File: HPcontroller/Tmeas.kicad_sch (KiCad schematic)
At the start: 8 parts

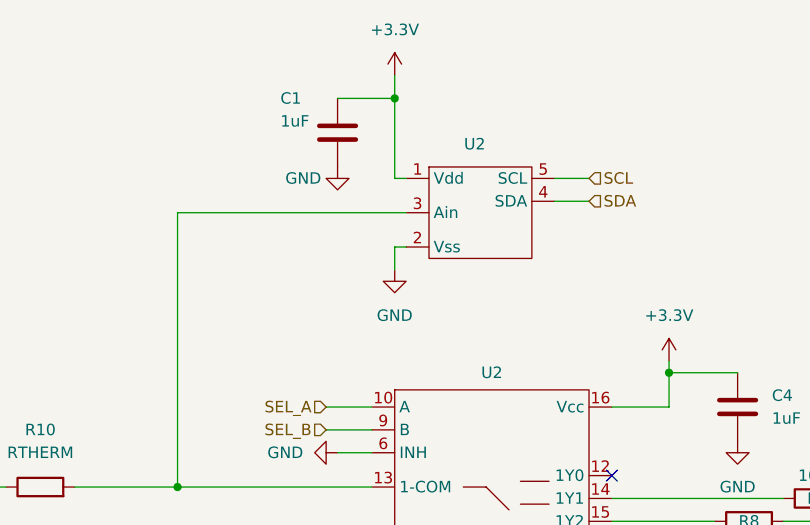
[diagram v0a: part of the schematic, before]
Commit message: started routing, finished footprintns
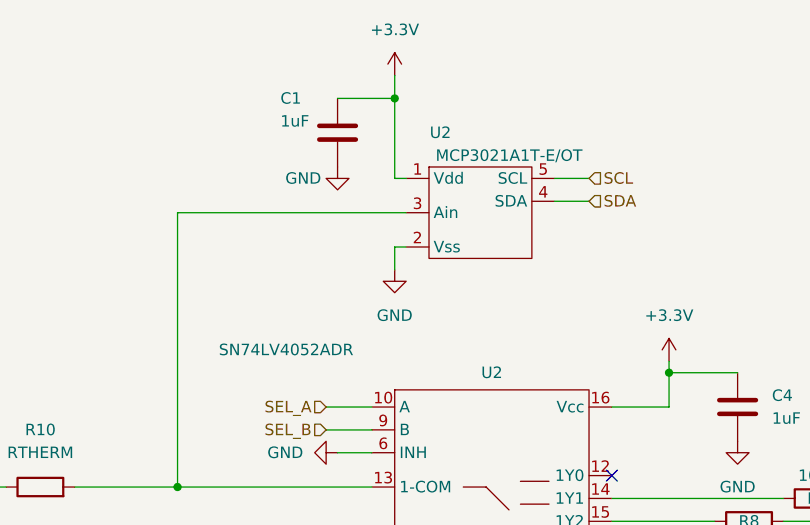
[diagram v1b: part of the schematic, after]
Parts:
- U2: value ~ -> MCP3021A1T-E/OT; footprint (none) -> Package_TO_SOT_SMD:SOT-23-5
- U2: value ~ -> SN74LV4052ADR; footprint (none) -> Package_SO:SOIC-16_3.9x9.9mm_P1.27mm
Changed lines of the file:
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@@
   )
   (symbol (lib_id "HPsym:MCP3021A1T-E/OT") (at 129.54 36.83 0) (unit 1)
-    (in_bom yes) (on_board yes) (dnp no) (fields_autoplaced)
-    (property "Reference" "U2" (at 129.54 34.29 0)
+    (in_bom yes) (on_board yes) (dnp no)
+    (property "Reference" "U2" (at 125.73 33.02 0)
       (effects (font (size 1.27 1.27)))
     )
-    (property "Value" "~" (at 123.825 36.83 0)
+    (property "Value" "MCP3021A1T-E/OT" (at 133.35 35.56 0)
       (effects (font (size 1.27 1.27)))
     )
-    (property "Footprint" "" (at 123.825 36.83 0)
+    (property "Footprint" "Package_TO_SOT_SMD:SOT-23-5" (at 123.825 36.83 0)
       (effects (font (size 1.27 1.27)) hide)
     )
@@
       (effects (font (size 1.27 1.27)))
     )
-    (property "Value" "~" (at 108.585 57.15 0)
+    (property "Value" "SN74LV4052ADR" (at 108.585 57.15 0)
       (effects (font (size 1.27 1.27)))
     )
-    (property "Footprint" "" (at 108.585 57.15 0)
+    (property "Footprint" "Package_SO:SOIC-16_3.9x9.9mm_P1.27mm" (at 108.585 57.15 0)
       (effects (font (size 1.27 1.27)) hide)
     )

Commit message: finished routing, moving on to heater
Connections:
- net +3.3V renamed +3V3
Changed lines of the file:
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@@
-    )
-  )
-  (symbol (lib_id "power:+3.3V") (at 66.04 63.5 0) (unit 1)
-    (in_bom yes) (on_board yes) (dnp no) (fields_autoplaced)
-    (property "Reference" "#PWR038" (at 66.04 67.31 0)
-      (effects (font (size 1.27 1.27)) hide)
-    )
-    (property "Value" "+3.3V" (at 66.04 58.42 0)
-      (effects (font (size 1.27 1.27)))
-    )
-    (property "Footprint" "" (at 66.04 63.5 0)
-      (effects (font (size 1.27 1.27)) hide)
-    )
-    (property "Datasheet" "" (at 66.04 63.5 0)
-      (effects (font (size 1.27 1.27)) hide)
-    )
-    (pin "1")
-    (instances
-      (project "HPcontroller"
-        (path "/e63e39d7-6ac0-4ffd-8aa3-1841a4541b55/1e79cfd4-57e0-46dc-a3a8-eabf19cd908e"
-          (reference "#PWR038") (unit 1)
-        )
-      )
     )
   )
@@
     )
   )
-  (symbol (lib_id "power:+3.3V") (at 151.13 58.42 0) (unit 1)
-    (in_bom yes) (on_board yes) (dnp no) (fields_autoplaced)
-    (property "Reference" "#PWR034" (at 151.13 62.23 0)
-      (effects (font (size 1.27 1.27)) hide)
-    )
-    (property "Value" "+3.3V" (at 151.13 53.34 0)
-      (effects (font (size 1.27 1.27)))
-    )
-    (property "Footprint" "" (at 151.13 58.42 0)
-      (effects (font (size 1.27 1.27)) hide)
-    )
-    (property "Datasheet" "" (at 151.13 58.42 0)
-      (effects (font (size 1.27 1.27)) hide)
-    )
-    (pin "1")
-    (instances
-      (project "HPcontroller"
-        (path "/e63e39d7-6ac0-4ffd-8aa3-1841a4541b55/1e79cfd4-57e0-46dc-a3a8-eabf19cd908e"
-          (reference "#PWR034") (unit 1)
+  (symbol (lib_id "power:+3V3") (at 66.04 63.5 0) (unit 1)
+    (in_bom yes) (on_board yes) (dnp no) (fields_autoplaced)
+    (property "Reference" "#PWR018" (at 66.04 67.31 0)
+      (effects (font (size 1.27 1.27)) hide)
+    )
+    (property "Value" "+3V3" (at 66.04 58.42 0)
+      (effects (font (size 1.27 1.27)))
+    )
+    (property "Footprint" "" (at 66.04 63.5 0)
+      (effects (font (size 1.27 1.27)) hide)
+    )
+    (property "Datasheet" "" (at 66.04 63.5 0)
+      (effects (font (size 1.27 1.27)) hide)
+    )
+    (pin "1")
+    (instances
+      (project "HPcontroller"
+        (path "/e63e39d7-6ac0-4ffd-8aa3-1841a4541b55/1e79cfd4-57e0-46dc-a3a8-eabf19cd908e"
+          (reference "#PWR018") (unit 1)
         )
       )
@@
     )
   )
+  (symbol (lib_id "power:+3V3") (at 151.13 58.42 0) (unit 1)
+    (in_bom yes) (on_board yes) (dnp no) (fields_autoplaced)
+    (property "Reference" "#PWR034" (at 151.13 62.23 0)
+      (effects (font (size 1.27 1.27)) hide)
+    )
+    (property "Value" "+3V3" (at 151.13 53.34 0)
+      (effects (font (size 1.27 1.27)))
+    )
+    (property "Footprint" "" (at 151.13 58.42 0)
+      (effects (font (size 1.27 1.27)) hide)
+    )
+    (property "Datasheet" "" (at 151.13 58.42 0)
+      (effects (font (size 1.27 1.27)) hide)
+    )
+    (pin "1")
+    (instances
+      (project "HPcontroller"
+        (path "/e63e39d7-6ac0-4ffd-8aa3-1841a4541b55/1e79cfd4-57e0-46dc-a3a8-eabf19cd908e"
+          (reference "#PWR034") (unit 1)
+        )
+      )
+    )
+  )
   (symbol (lib_id "power:GND") (at 171.45 82.55 0) (unit 1)
     (in_bom yes) (on_board yes) (dnp no) (fields_autoplaced)
@@
         (path "/e63e39d7-6ac0-4ffd-8aa3-1841a4541b55/1e79cfd4-57e0-46dc-a3a8-eabf19cd908e"
           (reference "#PWR035") (unit 1)
+        )
+      )
+    )
+  )
+  (symbol (lib_id "power:+3V3") (at 120.65 26.67 0) (unit 1)
+    (in_bom yes) (on_board yes) (dnp no) (fields_autoplaced)
+    (property "Reference" "#PWR038" (at 120.65 30.48 0)
+      (effects (font (size 1.27 1.27)) hide)
+    )
+    (property "Value" "+3V3" (at 120.65 21.59 0)
+      (effects (font (size 1.27 1.27)))
+    )
+    (property "Footprint" "" (at 120.65 26.67 0)
+      (effects (font (size 1.27 1.27)) hide)
+    )
+    (property "Datasheet" "" (at 120.65 26.67 0)
+      (effects (font (size 1.27 1.27)) hide)
+    )
+    (pin "1")
+    (instances
+      (project "HPcontroller"
+        (path "/e63e39d7-6ac0-4ffd-8aa3-1841a4541b55/1e79cfd4-57e0-46dc-a3a8-eabf19cd908e"
+          (reference "#PWR038") (unit 1)
         )
       )
@@
         )
       )
-    )
-  )
-  (symbol (lib_id "power:+3.3V") (at 120.65 26.67 0) (unit 1)
-    (in_bom yes) (on_board yes) (dnp no) (fields_autoplaced)
-    (property "Reference" "#PWR039" (at 120.65 30.48 0)
-      (effects (font (size 1.27 1.27)) hide)
-    )
-    (property "Value" "+3.3V" (at 120.65 21.59 0)
-      (effects (font (size 1.27 1.27)))
-    )
-    (property "Footprint" "" (at 120.65 26.67 0)
-      (effects (font (size 1.27 1.27)) hide)
-    )
-    (property "Datasheet" "" (at 120.65 26.67 0)
-      (effects (font (size 1.27 1.27)) hide)
-    )
-    (pin "1")
-    (instances
-      (project "HPcontroller"
-        (path "/e63e39d7-6ac0-4ffd-8aa3-1841a4541b55/1e79cfd4-57e0-46dc-a3a8-eabf19cd908e"
-          (reference "#PWR039") (unit 1)
-        )
-      )

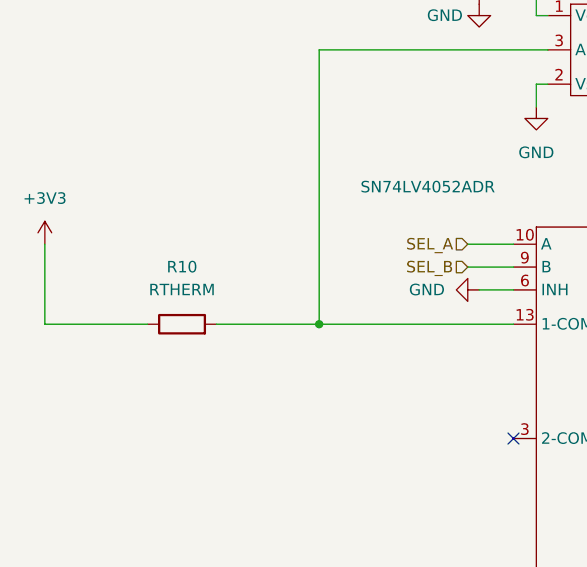
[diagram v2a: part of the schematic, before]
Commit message: worked on bom, orderables from dk are in
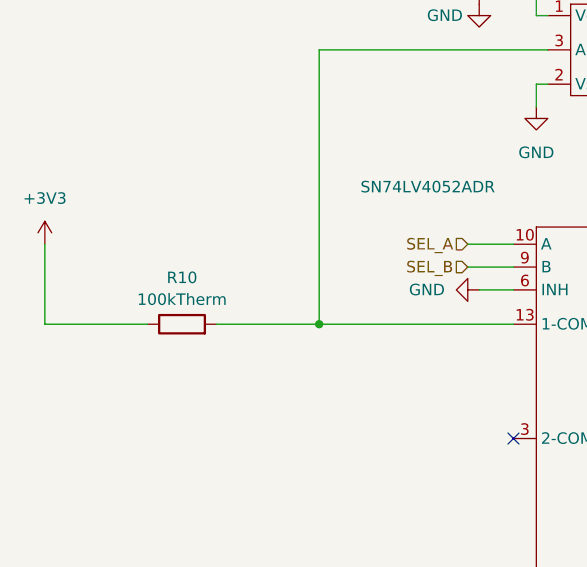
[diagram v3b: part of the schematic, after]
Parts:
- C1, C4: Digikey PN (none) -> 1276-1066-1-ND; MPN (none) -> CL21B105KAFNNNE
- R10: value RTHERM -> 100kTherm; MPN (none) -> 104NT-4-R025H42G
- R7: Digikey PN (none) -> RMCF0805FT100KCT-ND; MPN (none) -> RMCF0805FT100K
- R8: Digikey PN (none) -> RNCP0805FTD10K0CT-ND; MPN (none) -> RNCP0805FTD10K0
- R9: Digikey PN (none) -> RNCP0805FTD1K00CT-ND; MPN (none) -> RNCP0805FTD1K00
- U2: Digikey PN (none) -> MCP3021A1T-E/OTCT-ND; MPN (none) -> MCP3021A1T-E/OT
- U2: Digikey PN (none) -> 296-16707-1-ND; MPN (none) -> SN74LV4052ADR
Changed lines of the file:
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@@
   (symbol (lib_id "Device:R") (at 81.28 72.39 90) (unit 1)
     (in_bom yes) (on_board yes) (dnp no) (fields_autoplaced)
-    (property "Reference" "R10" (at 81.28 66.04 90)
-      (effects (font (size 1.27 1.27)))
-    )
-    (property "Value" "RTHERM" (at 81.28 68.58 90)
+    (property "Reference" "R10" (at 81.28 67.2297 90)
+      (effects (font (size 1.27 1.27)))
+    )
+    (property "Value" "100kTherm" (at 81.28 69.6539 90)
       (effects (font (size 1.27 1.27)))
     )
@@
     )
     (property "Datasheet" "~" (at 81.28 72.39 0)
+      (effects (font (size 1.27 1.27)) hide)
+    )
+    (property "MPN" "104NT-4-R025H42G" (at 81.28 72.39 0)
       (effects (font (size 1.27 1.27)) hide)
     )
@@
       (effects (font (size 1.27 1.27)) hide)
     )
+    (property "Digikey PN" "RNCP0805FTD1K00CT-ND" (at 152.4 78.74 0)
+      (effects (font (size 1.27 1.27)) hide)
+    )
+    (property "MPN" "RNCP0805FTD1K00" (at 152.4 78.74 0)
+      (effects (font (size 1.27 1.27)) hide)
+    )
     (pin "1")
     (pin "2")
@@
       (effects (font (size 1.27 1.27)) hide)
     )
+    (property "Digikey PN" "RNCP0805FTD10K0CT-ND" (at 160.02 76.2 0)
+      (effects (font (size 1.27 1.27)) hide)
+    )
+    (property "MPN" "RNCP0805FTD10K0" (at 160.02 76.2 0)
+      (effects (font (size 1.27 1.27)) hide)
+    )
     (pin "1")
     (pin "2")
@@
     )
     (property "Datasheet" "" (at 123.825 36.83 0)
+      (effects (font (size 1.27 1.27)) hide)
+    )
+    (property "Digikey PN" "MCP3021A1T-E/OTCT-ND" (at 129.54 36.83 0)
+      (effects (font (size 1.27 1.27)) hide)
+    )
+    (property "MPN" "MCP3021A1T-E/OT" (at 129.54 36.83 0)
       (effects (font (size 1.27 1.27)) hide)
     )
@@
       (effects (font (size 1.27 1.27)) hide)
     )
+    (property "Digikey PN" "RMCF0805FT100KCT-ND" (at 167.64 73.66 0)
+      (effects (font (size 1.27 1.27)) hide)
+    )
+    (property "MPN" "RMCF0805FT100K" (at 167.64 73.66 0)
+      (effects (font (size 1.27 1.27)) hide)
+    )
     (pin "1")
     (pin "2")
@@
     )
     (property "Datasheet" "" (at 108.585 57.15 0)
+      (effects (font (size 1.27 1.27)) hide)
+    )
+    (property "Digikey PN" "296-16707-1-ND" (at 130.81 77.47 0)
+      (effects (font (size 1.27 1.27)) hide)
+    )
+    (property "MPN" "SN74LV4052ADR" (at 130.81 77.47 0)
       (effects (font (size 1.27 1.27)) hide)
     )
@@
       (effects (font (size 1.27 1.27)) hide)
     )
+    (property "Digikey PN" "1276-1066-1-ND" (at 158.75 63.5 0)
+      (effects (font (size 1.27 1.27)) hide)
+    )
+    (property "MPN" "CL21B105KAFNNNE" (at 158.75 63.5 0)
+      (effects (font (size 1.27 1.27)) hide)
+    )
     (pin "1")
     (pin "2")
@@
       (effects (font (size 1.27 1.27)) hide)
     )
+    (property "Digikey PN" "1276-1066-1-ND" (at 114.3 33.02 0)
+      (effects (font (size 1.27 1.27)) hide)
+    )
+    (property "MPN" "CL21B105KAFNNNE" (at 114.3 33.02 0)
+      (effects (font (size 1.27 1.27)) hide)
+    )

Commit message: v3 routing
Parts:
- renumbered U2 to U6

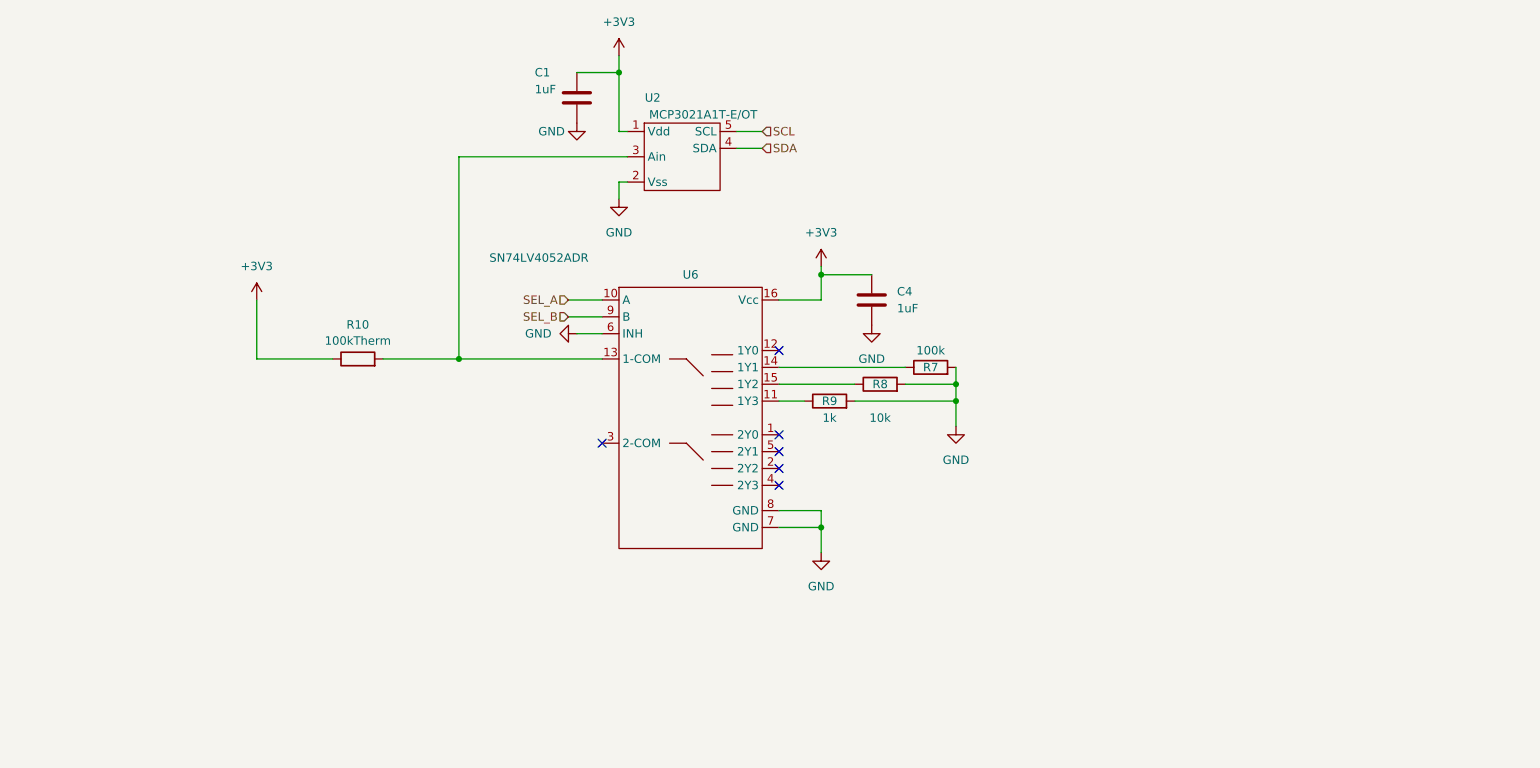
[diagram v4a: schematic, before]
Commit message: new temp circuit
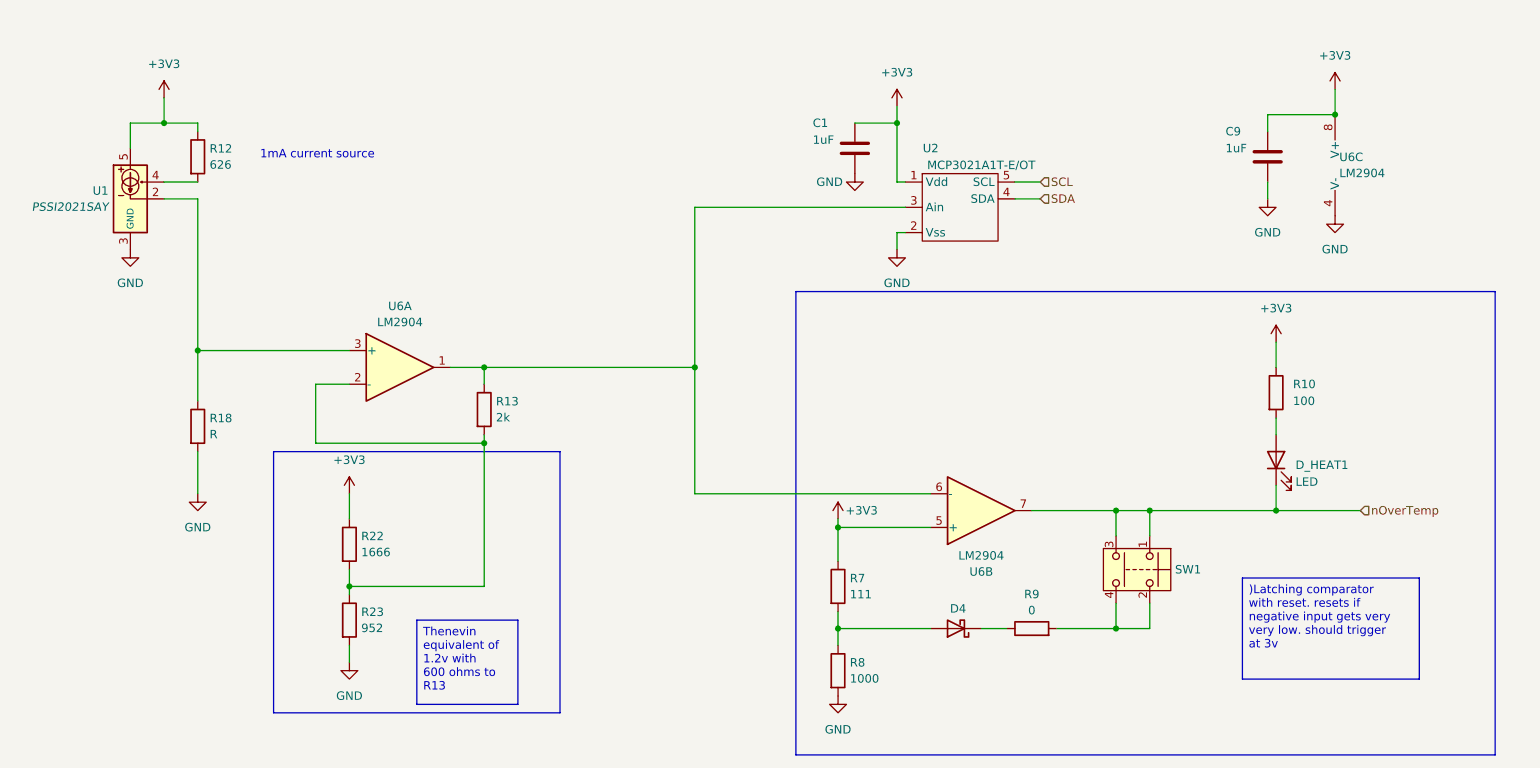
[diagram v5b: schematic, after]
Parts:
- removed C4: 1uF, Capacitor_SMD:C_0805_2012Metric_Pad1.18x1.45mm_HandSolder, symbol Device:C
- removed U6: SN74LV4052ADR, Package_SO:SOIC-16_3.9x9.9mm_P1.27mm, symbol HPsym:SN74LV4052ADR
- added C9: 1uF, Capacitor_SMD:C_0805_2012Metric_Pad1.18x1.45mm_HandSolder, symbol Device:C
- added D4: D_Schottky, symbol Device:D_Schottky
- added D_HEAT1: LED, LED_SMD:LED_0603_1608Metric_Pad1.05x0.95mm_HandSolder, symbol Device:LED
- added R12: 626, Resistor_SMD:R_0603_1608Metric, symbol Device:R
- added R13: 2k, Resistor_SMD:R_0603_1608Metric, symbol Device:R
- added R18: R, symbol Device:R
- added R22: 1666, Resistor_SMD:R_0603_1608Metric, symbol Device:R
- added R23: 952, Resistor_SMD:R_0603_1608Metric, symbol Device:R
- added SW1: SW_Push_Dual, symbol Switch:SW_Push_Dual
- added U1: PSSI2021SAY, Package_TO_SOT_SMD:SOT-353_SC-70-5, symbol Reference_Current:PSSI2021SAY
- added U6: LM2904, hotplate_Library:MINISO8_3P1X3P2X0P65_STM, symbol Amplifier_Operational:LM2904
- R10: value 100kTherm -> 100; footprint Resistor_SMD:R_0805_2012Metric_Pad1.20x1.40mm_HandSolder -> Resistor_SMD:R_0603_1608Metric; Digikey PN (none) -> A130128CT-ND; MPN 104NT-4-R025H42G -> CRGCQ0805J100R
- R7: value 100k -> 111; footprint Resistor_SMD:R_0805_2012Metric_Pad1.20x1.40mm_HandSolder -> Resistor_SMD:R_0603_1608Metric; Digikey PN RMCF0805FT100KCT-ND -> (none); MPN RMCF0805FT100K -> (none)
- R8: value 10k -> 1000; footprint Resistor_SMD:R_0805_2012Metric_Pad1.20x1.40mm_HandSolder -> Resistor_SMD:R_0603_1608Metric; Digikey PN RNCP0805FTD10K0CT-ND -> (none); MPN RNCP0805FTD10K0 -> (none)
- R9: value 1k -> 0; footprint Resistor_SMD:R_0805_2012Metric_Pad1.20x1.40mm_HandSolder -> Resistor_SMD:R_0603_1608Metric; Digikey PN RNCP0805FTD1K00CT-ND -> (none); MPN RNCP0805FTD1K00 -> (none)
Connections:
- net +3V3: now also R7.1, C9.1, R12.1, R22.1, U1.5, U6.5 (+), U6.8 (V+)
- net GND: now also C9.2, R18.2, R23.2, U1.3 (GND), U6.4 (V-); no longer R7.2, R9.2
- net at U2.3 (Ain): now also R13.1, U6.1, U6.6 (-); no longer R10.2
- net at R9.1: now also D4.1 (K)
- net at R8.1: now also R7.2, D4.2 (A)
- new net: R13.2, R22.2, R23.1, U6.2 (-)
- new net: R12.2, U1.4
- new net: R18.1, U1.2, U6.3 (+)
- new net: D_HEAT1.2 (A), R10.2
- new net: R9.2, SW1.2, SW1.4
- new net nOverTemp: D_HEAT1.1 (K), SW1.1, SW1.3, U6.7
- no-connect marks 6 -> 0
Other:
- note added: "1mA current source"
- moved on the sheet: C1, U2

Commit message: finished temp meas stuff, laying out
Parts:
- removed D4: D_Schottky, symbol Device:D_Schottky
- removed SW1: SW_Push_Dual, symbol Switch:SW_Push_Dual
- added C4: 1uF, Capacitor_SMD:C_0805_2012Metric, symbol Device:C
- added D2: BAR43FILM, Package_TO_SOT_SMD:SOT-23, symbol Diode:BAR43FILM
- added SW1: SW_SPST, hotplate_Library:SW_EVQ-P7J01P, symbol Switch:SW_SPST
- added TP4, TP5, TP6, TP7, TP9: TestPoint, TestPoint:TestPoint_Pad_D1.5mm, symbol Connector:TestPoint
- C1, C9: footprint Capacitor_SMD:C_0805_2012Metric_Pad1.18x1.45mm_HandSolder -> Capacitor_SMD:C_0805_2012Metric
- R12: MPN (none) -> RT0603BRD07626RL
- R13: value 2k -> 1210; MPN (none) -> RC0603FR-071K21L
- R18: value R -> RTD PT1000; footprint (none) -> Resistor_SMD:R_0805_2012Metric; MPN (none) -> 30200145
- R22: value 1666 -> 1300; MPN (none) -> RC0603FR-071K3L
- R23: value 952 -> 1020; MPN (none) -> ERJ-3EKF1021V
- R7: value 111 -> 120; MPN (none) -> ERJ-3EKF1200V
- R8: value 1000 -> 1200; MPN (none) -> CR0603-FX-1203ELF
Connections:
- net +3V3: now also C4.1; no longer U6.5 (+)
- net GND: now also C4.2, SW1.1 (A)
- net nOverTemp: now also R9.2, TP9.1
- net at R7.2, R8.1: now also U6.5 (+), D2.1 (A), TP7.1
- net at R13.1, U2.3 (Ain), U6.1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: now also SW1.2 (B), TP5.1
- net at R13.2, R22.2, R23.1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: now also TP6.1
- net at R18.1, U1.2, U6.3 (+): now also TP4.1
- net at R9.1: now also D2.3 (K)
